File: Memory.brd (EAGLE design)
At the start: 106.7 x 37.8 mm, 8 parts, among them IC1 AT28C256ZIF, IC2 HM62256DIP

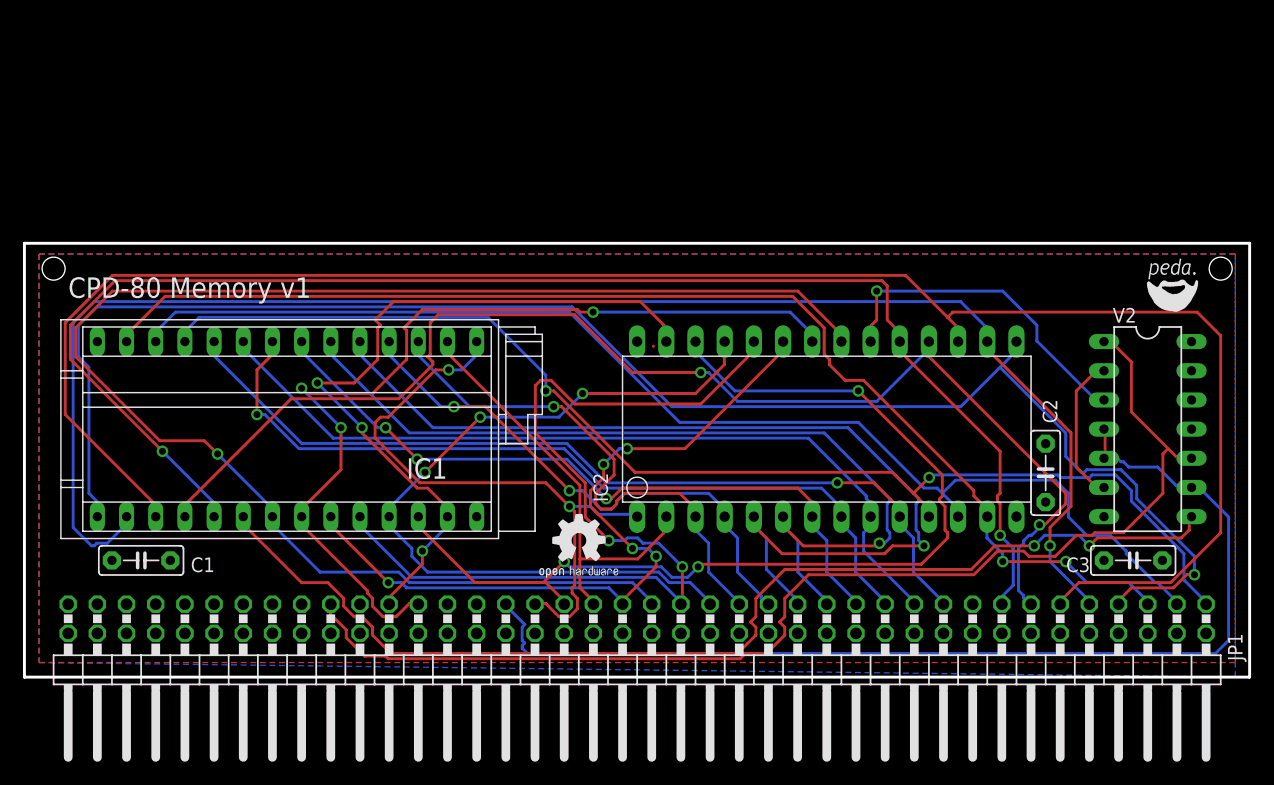
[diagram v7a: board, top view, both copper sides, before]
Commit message: Fix Memory Mapping inversely. Move Text on Muddi
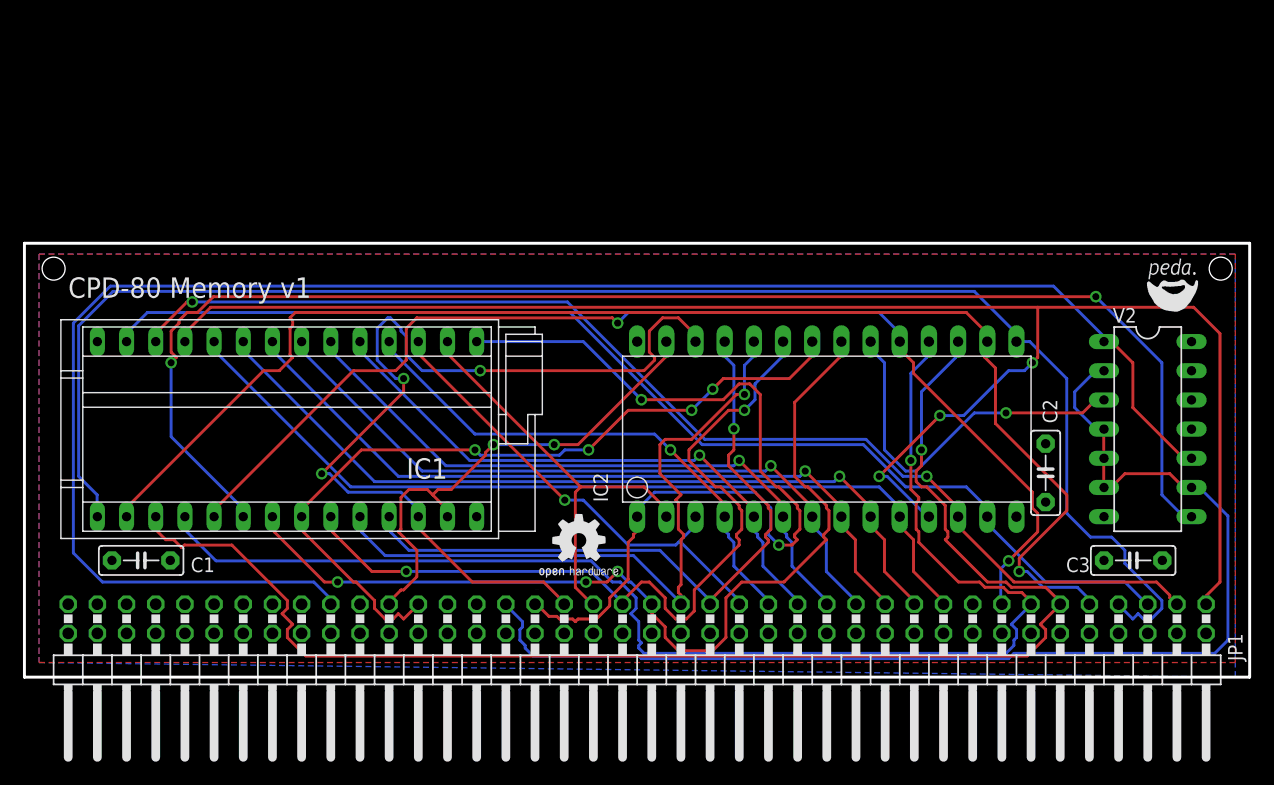
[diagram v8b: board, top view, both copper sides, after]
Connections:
- removed net N$4: V2.2, V2.6
- net A15: now also V2.2, V2.6
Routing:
- net A10: track 132.9 -> 82.3 mm, vias 1 -> 3
- net !MREQ: track 102.4 -> 152.0 mm
- net D5: track 161.3 -> 123.4 mm, vias 0 -> 1
- net D0: track 107.5 -> 145.1 mm, vias 2 -> 3
- net A5: track 85.8 -> 51.1 mm
- net D7: track 127.8 -> 100.3 mm
- net N$2: track 97.3 -> 124.0 mm
- net A14: track 53.3 -> 77.7 mm
- net A4: track 79.0 -> 56.4 mm
- net !WR: track 64.7 -> 43.8 mm, vias 3 -> 2
- net A9: track 81.7 -> 61.5 mm, vias 2 -> 1
- net D4: track 135.1 -> 119.2 mm
- net N$4: track 12.9 -> 0.00 mm
- net !RD: track 80.4 -> 68.2 mm, vias 3 -> 4
- net A15: track 93.3 -> 103.7 mm
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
